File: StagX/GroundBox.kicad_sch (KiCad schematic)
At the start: 0 parts

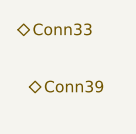
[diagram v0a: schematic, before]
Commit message: feat(RearLoom): made progress with rear elec box. TSAL LED conns missing
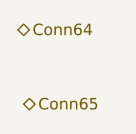
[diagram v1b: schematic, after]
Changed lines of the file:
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@@
 (kicad_sch (version 20230121) (generator eeschema)
   (paper "A4")
-  (hierarchical_label "Conn33" (shape bidirectional) (at 123.19 64.135 0) (fields_autoplaced)
+  (hierarchical_label "Conn64" (shape bidirectional) (at 123.19 64.135 0) (fields_autoplaced)
     (effects (font (size 1.27 1.27)) (justify left))
   )
-  (hierarchical_label "Conn39" (shape bidirectional) (at 124.46 70.485 0) (fields_autoplaced)
+  (hierarchical_label "Conn65" (shape bidirectional) (at 123.825 72.39 0) (fields_autoplaced)
     (effects (font (size 1.27 1.27)) (justify left))
   )

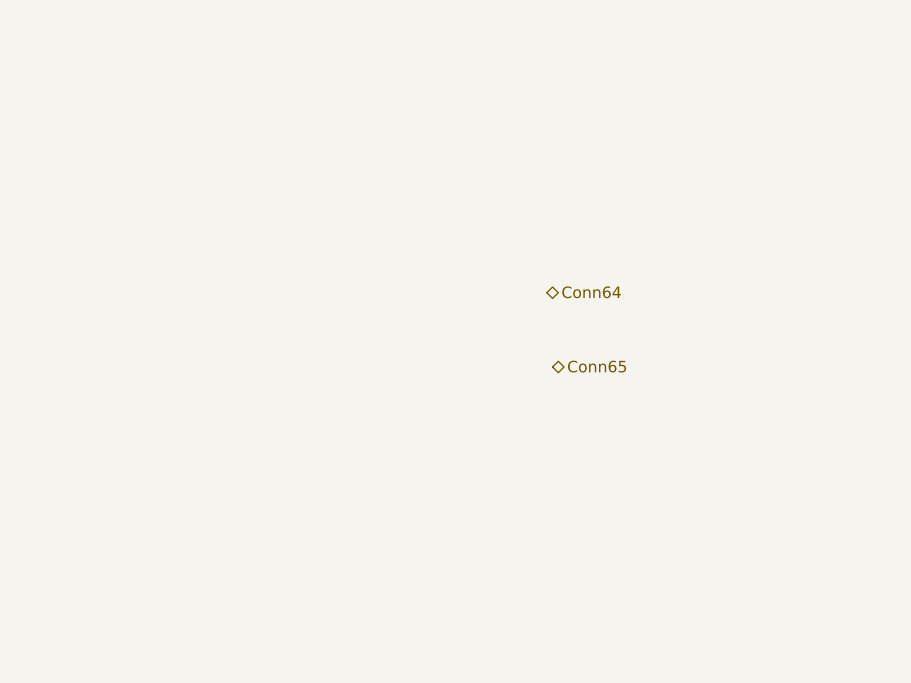
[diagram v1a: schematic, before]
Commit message: feat(RearLoom): completed Rear Electronics Box
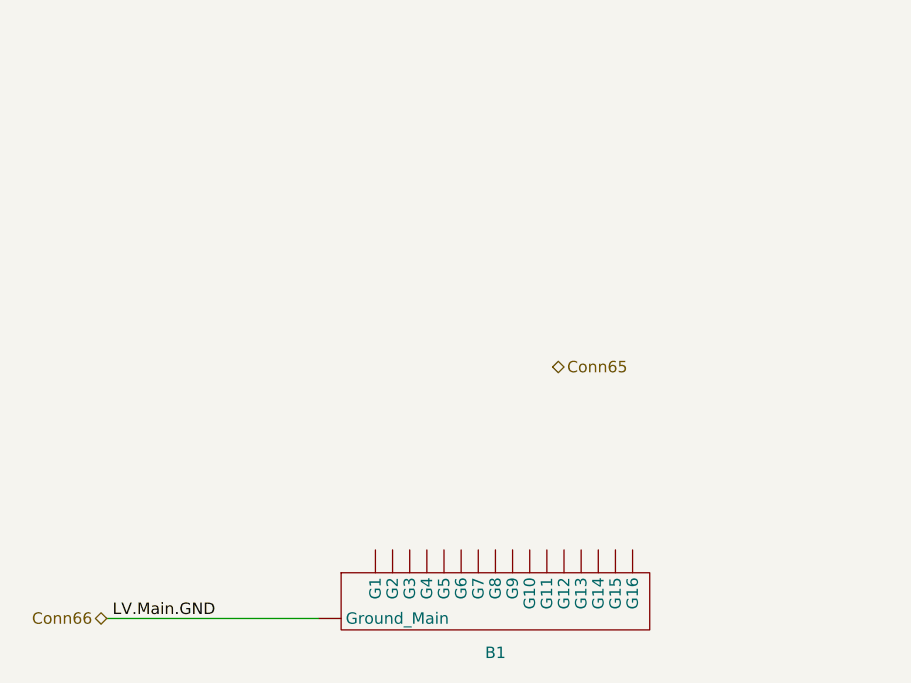
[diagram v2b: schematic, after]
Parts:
- added B1: ~, symbol Connectors_SUFST:Ground
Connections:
- new net Conn66: B1. (Ground_Main)
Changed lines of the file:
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@@
 (kicad_sch (version 20230121) (generator eeschema)
   (paper "A4")
-  (hierarchical_label "Conn64" (shape bidirectional) (at 123.19 64.135 0) (fields_autoplaced)
-    (effects (font (size 1.27 1.27)) (justify left))
+  (wire (pts (xy 74.295 100.33) (xy 97.79 100.33))
+    (stroke (width 0) (type default))
+  )
+  (label "LV.Main.GND" (at 74.93 100.33 0) (fields_autoplaced)
+    (effects (font (size 1.27 1.27)) (justify left bottom))
+  )
+  (hierarchical_label "Conn66" (shape bidirectional) (at 74.295 100.33 180) (fields_autoplaced)
+    (effects (font (size 1.27 1.27)) (justify right))
   )
   (hierarchical_label "Conn65" (shape bidirectional) (at 123.825 72.39 0) (fields_autoplaced)
     (effects (font (size 1.27 1.27)) (justify left))
   )
+  (symbol (lib_id "Connectors_SUFST:Ground") (at 117.475 92.075 0) (unit 1)
+    (in_bom yes) (on_board yes) (dnp no) (fields_autoplaced)
+    (property "Reference" "B1" (at 117.475 104.14 0)
+      (effects (font (size 1.27 1.27)))
+    )
+    (property "Value" "~" (at 127.635 92.71 0)
+      (effects (font (size 1.27 1.27)))
+    )
+    (property "Footprint" "" (at 127.635 92.71 0)
+      (effects (font (size 1.27 1.27)) hide)
+    )
+    (property "Datasheet" "" (at 127.635 92.71 0)
+      (effects (font (size 1.27 1.27)) hide)
+    )
+    (pin "")
+    (pin "")
+    (pin "")
+    (pin "")
+    (pin "")
+    (pin "")
+    (pin "")
+    (pin "")
+    (pin "")
+    (pin "")
+    (pin "")
+    (pin "")
+    (pin "")
+    (pin "")
+    (pin "")
+    (pin "")
+    (pin "")
+    (instances
+      (project "StagX"
+        (path "/f802a14a-9970-4775-97a5-629bebb8e9f9/8cd03b79-9b82-4468-9f8b-8ea849e7dcc8"
+          (reference "B1") (unit 1)
+        )
+      )
+    )
+  )
 )

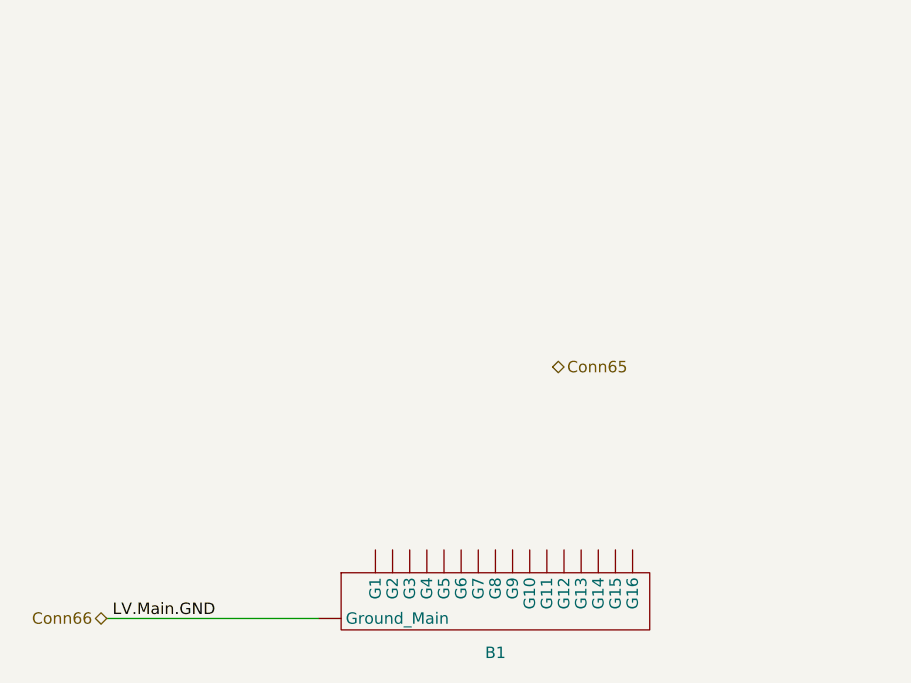
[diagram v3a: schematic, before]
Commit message: feat(RearLoom): PWR and GND complete. progress on top-level
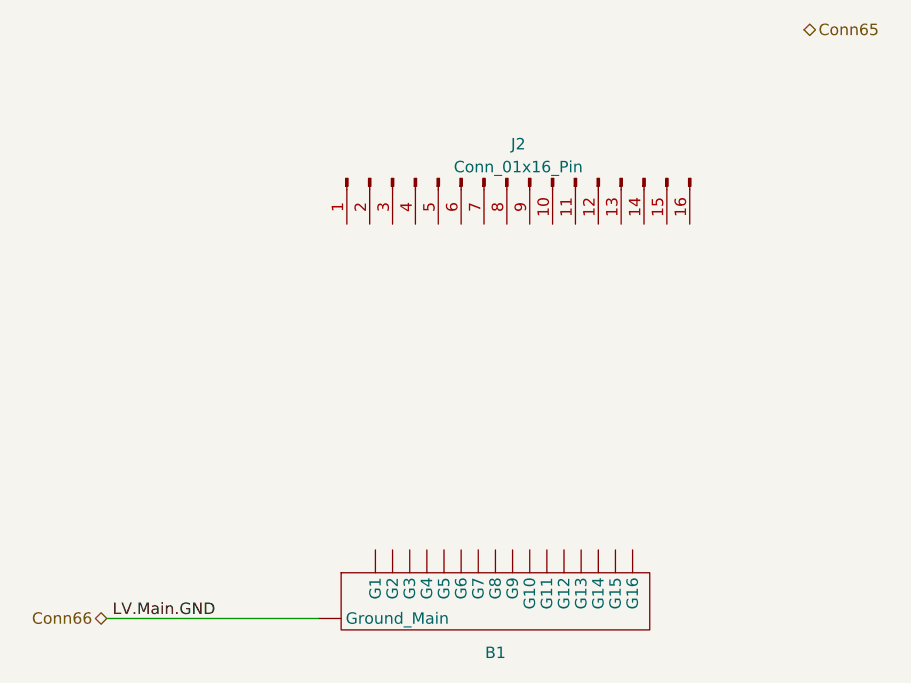
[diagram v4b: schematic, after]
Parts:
- added J2: Conn_01x16_Pin, symbol Connector:Conn_01x16_Pin
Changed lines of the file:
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@@
     (effects (font (size 1.27 1.27)) (justify right))
   )
-  (hierarchical_label "Conn65" (shape bidirectional) (at 123.825 72.39 0) (fields_autoplaced)
+  (hierarchical_label "Conn65" (shape bidirectional) (at 151.765 34.925 0) (fields_autoplaced)
     (effects (font (size 1.27 1.27)) (justify left))
   )
@@
         )
       )
+    )
+  )
+  (symbol (lib_id "Connector:Conn_01x16_Pin") (at 118.745 51.435 90) (mirror x) (unit 1)
+    (in_bom yes) (on_board yes) (dnp no) (fields_autoplaced)
+    (property "Reference" "J2" (at 120.015 47.625 90)
+      (effects (font (size 1.27 1.27)))
+    )
+    (property "Value" "Conn_01x16_Pin" (at 120.015 50.165 90)
+      (effects (font (size 1.27 1.27)))
+    )
+    (property "Footprint" "" (at 118.745 51.435 0)
+      (effects (font (size 1.27 1.27)) hide)
+    )
+    (property "Datasheet" "~" (at 118.745 51.435 0)
+      (effects (font (size 1.27 1.27)) hide)
+    )
+    (pin "1")
+    (pin "10")
+    (pin "11")
+    (pin "12")
+    (pin "13")
+    (pin "14")
+    (pin "15")
+    (pin "16")
+    (pin "2")
+    (pin "3")
+    (pin "4")
+    (pin "5")
+    (pin "6")
+    (pin "7")
+    (pin "8")
+    (pin "9")
+    (instances
+      (project "StagX"
+        (path "/f802a14a-9970-4775-97a5-629bebb8e9f9/8cd03b79-9b82-4468-9f8b-8ea849e7dcc8"
+          (reference "J2") (unit 1)
+        )
+      )
